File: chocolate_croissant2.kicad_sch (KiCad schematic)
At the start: 4 parts, among them U1 Pico

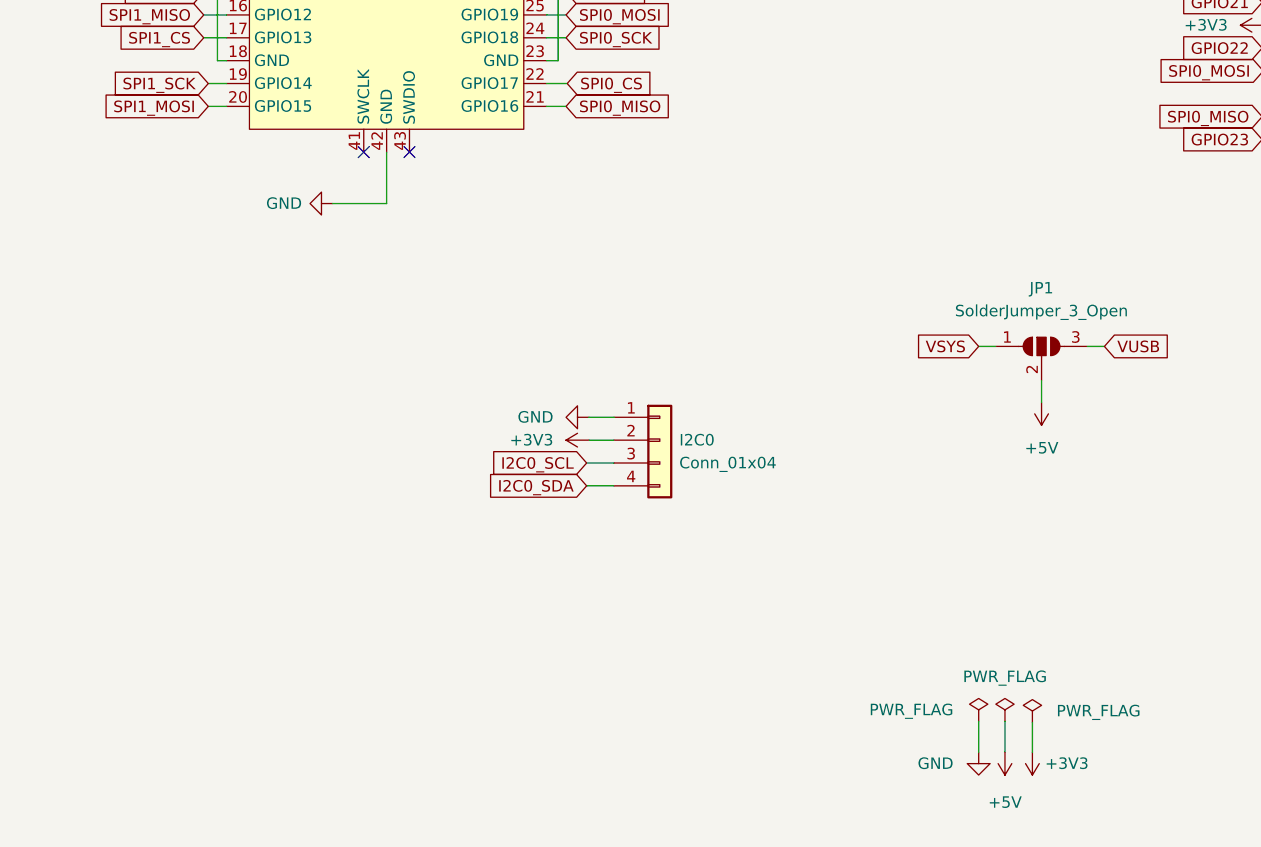
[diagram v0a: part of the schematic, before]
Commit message: SPI breakouts and new images.
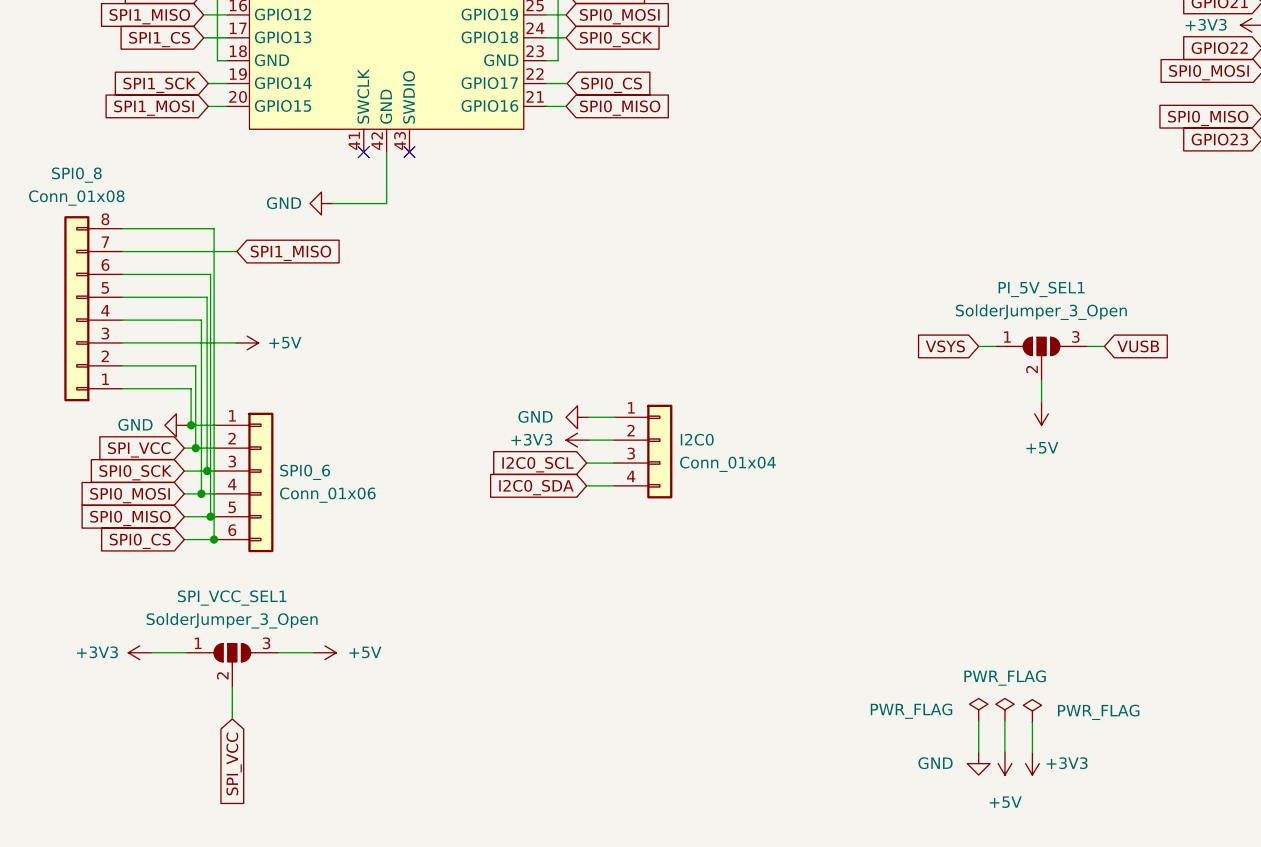
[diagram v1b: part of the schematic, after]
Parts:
- added SPI0_6: Conn_01x06, Connector_PinHeader_2.54mm:PinHeader_1x06_P2.54mm_Vertical, symbol Connector_Generic:Conn_01x06
- added SPI0_8: Conn_01x08, Connector_PinHeader_2.54mm:PinHeader_1x08_P2.54mm_Vertical, symbol Connector_Generic:Conn_01x08
- added SPI_VCC_SEL1: SolderJumper_3_Open, Jumper:SolderJumper-3_P1.3mm_Open_RoundedPad1.0x1.5mm_NumberLabels, symbol Jumper:SolderJumper_3_Open
- renumbered JP1 to PI_5V_SEL1
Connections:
- net +3V3: now also SPI_VCC_SEL1.1 (A)
- net +5V: now also SPI0_8.3 (Pin_3), SPI_VCC_SEL1.3 (B)
- net GND: now also SPI0_6.1 (Pin_1), SPI0_8.1 (Pin_1)
- net SPI0_CS: now also SPI0_6.6 (Pin_6), SPI0_8.8 (Pin_8)
- net SPI0_MISO: now also SPI0_6.5 (Pin_5), SPI0_8.6 (Pin_6)
- net SPI0_MOSI: now also SPI0_6.4 (Pin_4), SPI0_8.4 (Pin_4)
- net SPI0_SCK: now also SPI0_6.3 (Pin_3), SPI0_8.5 (Pin_5)
- net SPI1_MISO: now also SPI0_8.7 (Pin_7)
- new net SPI_VCC: SPI0_6.2 (Pin_2), SPI0_8.2 (Pin_2), SPI_VCC_SEL1.2 (C)

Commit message: Adding some more stuff, more documentation in the README etc.
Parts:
- added DEBUG1, I2C0QT1: QWIIC_CONNECTORJS-1MM, Connector_JST:JST_SH_SM04B-SRSS-TB_1x04-1MP_P1.00mm_Horizontal, symbol SparkFun-Connectors:QWIIC_CONNECTORJS-1MM
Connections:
- net +3V3: now also SPI0_8.2 (Pin_2), DEBUG1.2 (VCC), I2C0QT1.2 (VCC)
- net GND: now also DEBUG1.1 (GND), I2C0QT1.1 (GND)
- net I2C0_SCL: now also I2C0QT1.4 (SCL)
- net I2C0_SDA: now also I2C0QT1.3 (SDA)
- net SPI_VCC: no longer SPI0_8.2 (Pin_2)
- net DEBUG_CLK: now reaches U1.41 (SWCLK)
- net DEBUG_CLK: now also DEBUG1.4 (SCL)
- net DEBUG_DATA: now reaches U1.43 (SWDIO)
- net DEBUG_DATA: now also DEBUG1.3 (SDA)
- no-connect marks 6 -> 4
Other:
- company: (none) -> Robotika
- title: (none) -> Chocolate Croissant
- moved on the sheet: I2C0, PI_5V_SEL1, RP1, SPI0_6, SPI0_8, SPI_VCC_SEL1, U1

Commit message: KiCad 7 plus local footprints and symbols.
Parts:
- RP1: footprint Raspberry-Pi-4-library-for-kicad:raspberrypi_2_3 -> chocolate_croissant:raspberrypi_2_3; symbol Raspberry_Pi_2_or_3:Raspberry_Pi_2_3 -> chocolate_croissant:Raspberry_Pi_2_3
- U1: footprint RPi_Pico:RPi_Pico_SMD_TH -> chocolate_croissant:RPi_Pico_SMD_TH; symbol MCU_RaspberryPi_and_Boards:Pico -> chocolate_croissant:Pico
